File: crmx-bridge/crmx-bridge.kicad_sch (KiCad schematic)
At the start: 76 parts, among them IC101 ESP32-S3-WROOM-1U-N4R2, J101 Conn_01x18_Pin, J102 NC3FAAH2, J103 TYPEC-304S-ACP16, J104 NC3MAAH, J105 Conn_01x02_Pin, J106 Conn_01x18_Socket, Q101 DMPH4029LFGQ-13, Q102 AO3400A, U101 TIMOTWO, U102 AP63200WU, U103 ISO3088DW, U104 SRV05-4, U105 ISO3088DW

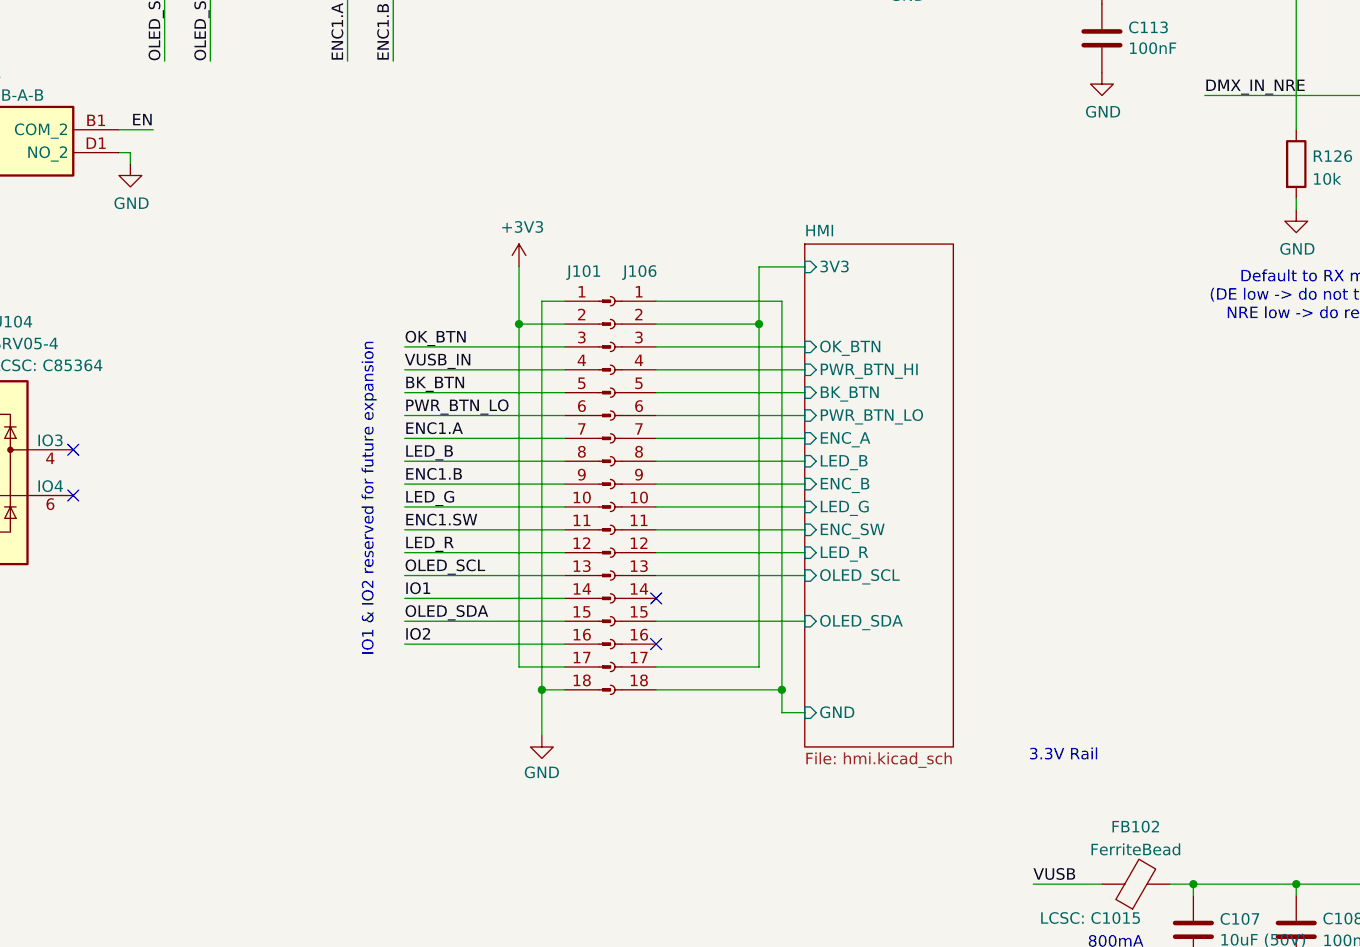
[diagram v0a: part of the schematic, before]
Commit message: updated to use FPC cable
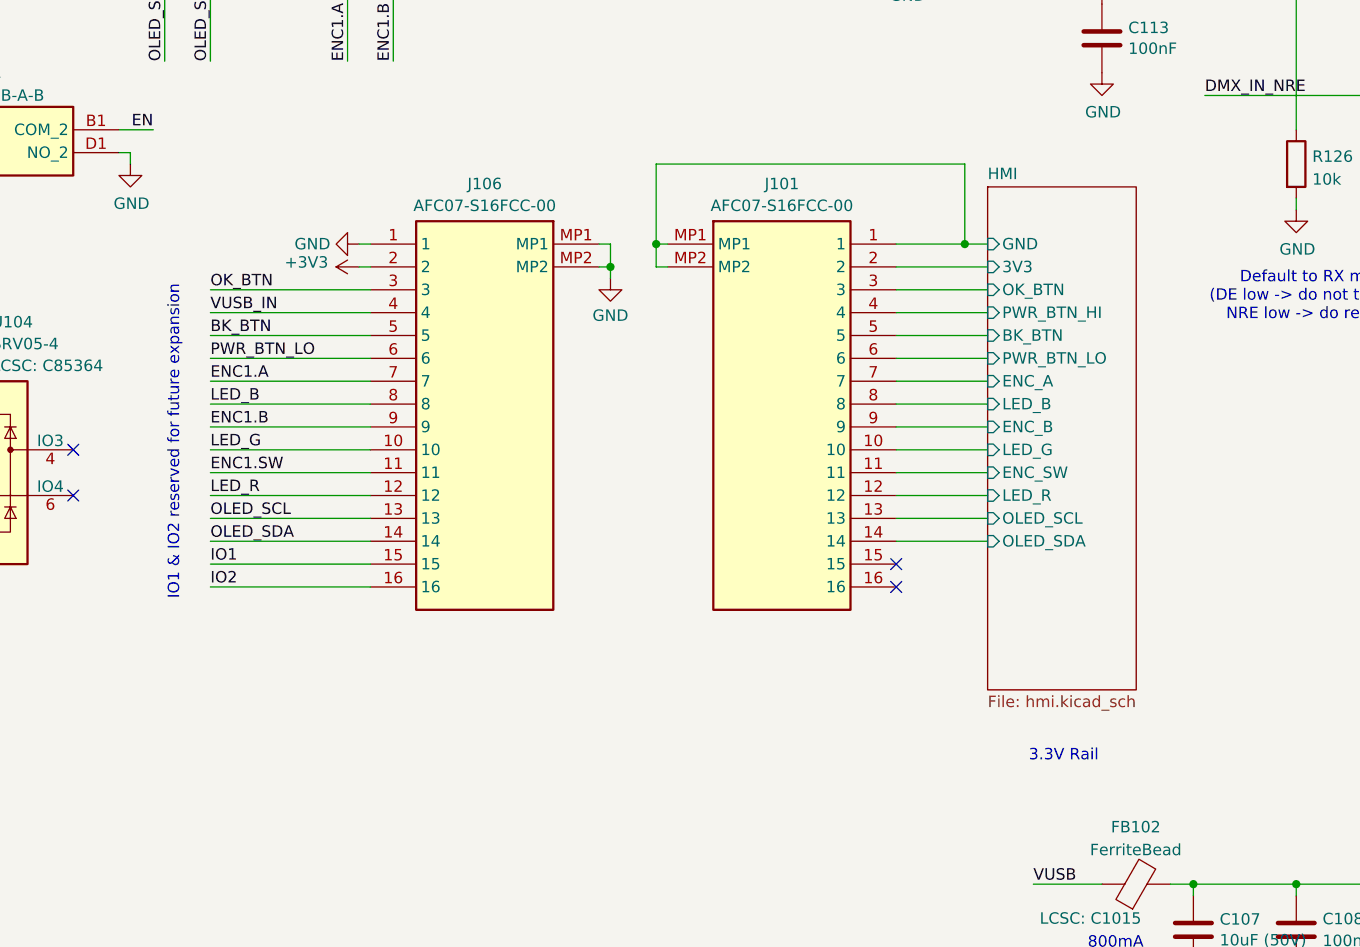
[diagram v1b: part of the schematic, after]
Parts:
- removed J101: Conn_01x18_Pin, Connector_PinSocket_1.27mm:PinSocket_2x09_P1.27mm_Vertical, symbol Connector:Conn_01x18_Pin
- removed J106: Conn_01x18_Socket, Connector_PinHeader_1.27mm:PinHeader_2x09_P1.27mm_Vertical, symbol Connector:Conn_01x18_Socket
- added J101, J106: AFC07-S16FCC-00, AFC07-S16FCC-00:AFC07S16FCC00, symbol AFC07-S16FCC-00:AFC07-S16FCC-00
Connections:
- net +3V3: now also J106.2
- net BK_BTN: now also J106.5
- net ENC1.A: now also J106.7
- net ENC1.B: now also J106.9
- net ENC1.SW: now also J106.11
- net GND: now also J106.1, J106.MP1, J106.MP2
- net HMI/3V3: now also J101.2
- net HMI/BK_BTN: now also J101.5
- net HMI/ENC_A: now also J101.7
- net HMI/ENC_B: now also J101.9
- net HMI/ENC_SW: now also J101.11
- net HMI/GND: now also J101.1, J101.MP1, J101.MP2
- net HMI/LED_B: now also J101.8
- net HMI/LED_G: now also J101.10
- net HMI/LED_R: now also J101.12
- net HMI/OK_BTN: now also J101.3
- net HMI/OLED_SCL: now also J101.13
- net HMI/OLED_SDA: now also J101.14
- net HMI/PWR_BTN_HI: now also J101.4
- net HMI/PWR_BTN_LO: now also J101.6
- net IO1: now also J106.15
- net IO2: now also J106.16
- net LED_B: now also J106.8
- net LED_G: now also J106.10
- net LED_R: now also J106.12
- net OK_BTN: now also J106.3
- net OLED_SCL: now also J106.13
- net OLED_SDA: now also J106.14
- net PWR_BTN_LO: now also J106.6
- net VUSB_IN: now also J106.4

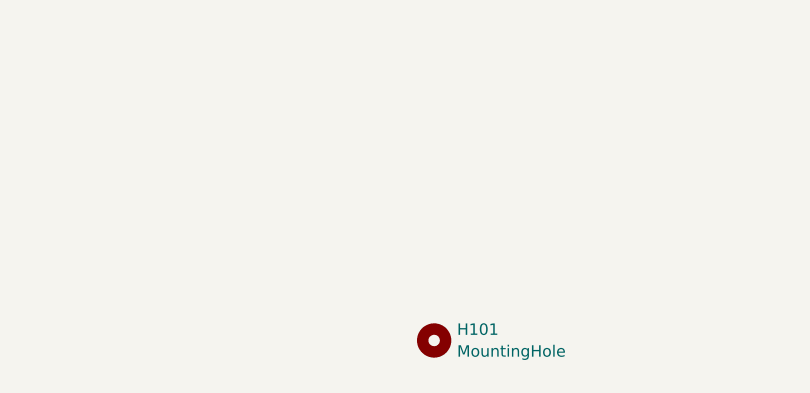
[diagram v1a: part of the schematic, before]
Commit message: Updated 3d models
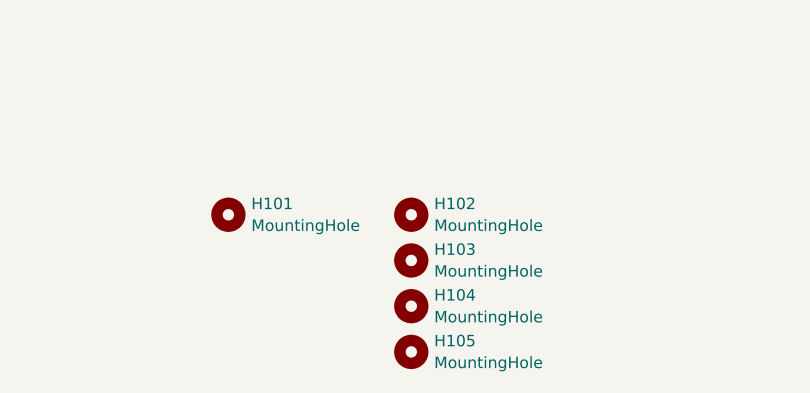
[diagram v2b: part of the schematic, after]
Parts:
- added H102, H103, H104, H105: MountingHole, MountingHole:MountingHole_3.2mm_M3, symbol Mechanical:MountingHole
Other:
- moved on the sheet: H101

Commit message: before rearranging
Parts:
- removed J103: TYPEC-304S-ACP16, LIB_TYPEC-304S-ACP16:TYPEC304SACP16, symbol TYPEC-304S-ACP16:TYPEC-304S-ACP16
- removed PS101, PS102: TEA_1-0505, Converter_DCDC:Converter_DCDC_TRACO_TEA1-xxxxE_THT, symbol Converter_DCDC:TEA1-0505E
- added J103: USB_C_Receptacle_USB2.0_16P, Connector_USB:USB_C_Receptacle_HRO_TYPE-C-31-M-12, symbol Connector:USB_C_Receptacle_USB2.0_16P
- added R125: 10R (1%), Resistor_SMD:R_0603_1608Metric, symbol Device:R
- added U106, U107: TEA1-0505, Converter_DCDC:Converter_DCDC_TRACO_TEA1-xxxx_THT, symbol Converter_DCDC:TEA1-0505
- IC101: LCSC (none) -> C3013942
- Q101: value DMPH4029LFGQ-13 -> DMP4025SFGQ-13; LCSC (none) -> C461091
- Q102: LCSC (none) -> C20917
- R103: value 133R (2%) -> 120R (1%); LCSC (none) -> C22787
- R104, R105: value 562R (2%) -> 560R (1%); LCSC (none) -> C23204
- R123: LCSC (none) -> C22787
- R132, R137, R138, R139, R140: value 50R -> 49R9; LCSC (none) -> C25120
- R134: LCSC C17168 -> (none)
- U103, U105: LCSC (none) -> C39386
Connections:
- net DMX_OUT_N: now also R125.2; no longer R103.2
- net GND: now also J103.A1 (GND), J103.A12 (GND), J103.B1 (GND), J103.B12 (GND), J103.S1 (SHIELD), U106.1 (-Vin), U107.1 (-Vin)
- net GND_ISO_1: now also U106.3 (-Vout)
- net GND_ISO_2: now also U107.3 (-Vout)
- net USB_CC1: now also J103.A5 (CC1)
- net USB_CC2: now also J103.B5 (CC2)
- net USB_DN: now also J103.A7 (D-), J103.B7 (D-)
- net USB_DP: now also J103.A6 (D+), J103.B6 (D+)
- net VCC_ISO_1: now also U106.4 (+Vout)
- net VCC_ISO_2: now also U107.4 (+Vout)
- net VUSB: now also U106.2 (+Vin), U107.2 (+Vin)
- net VUSB_IN: now also J103.A4 (VBUS), J103.A9 (VBUS), J103.B4 (VBUS), J103.B9 (VBUS)
- new net: R103.2, R125.1
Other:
- note added: "Line bias network to be RDM compliant https://getdlight.com/media/kunena/attachments/42/ANSI_E1-20_2010.pdf Ideal: 562 - 133 - 562"
- note removed: "Line bias network to be RDM compliant https://getdlight.com/media/kunena/attachments/42/ANSI_E1-20_2010.pdf"
- note removed: "TODO: - Monitor CC1 & CC2 voltages? - Make all resistors that can be 0402"
- moved on the sheet: J101, J106, R104, R105, R119, R120

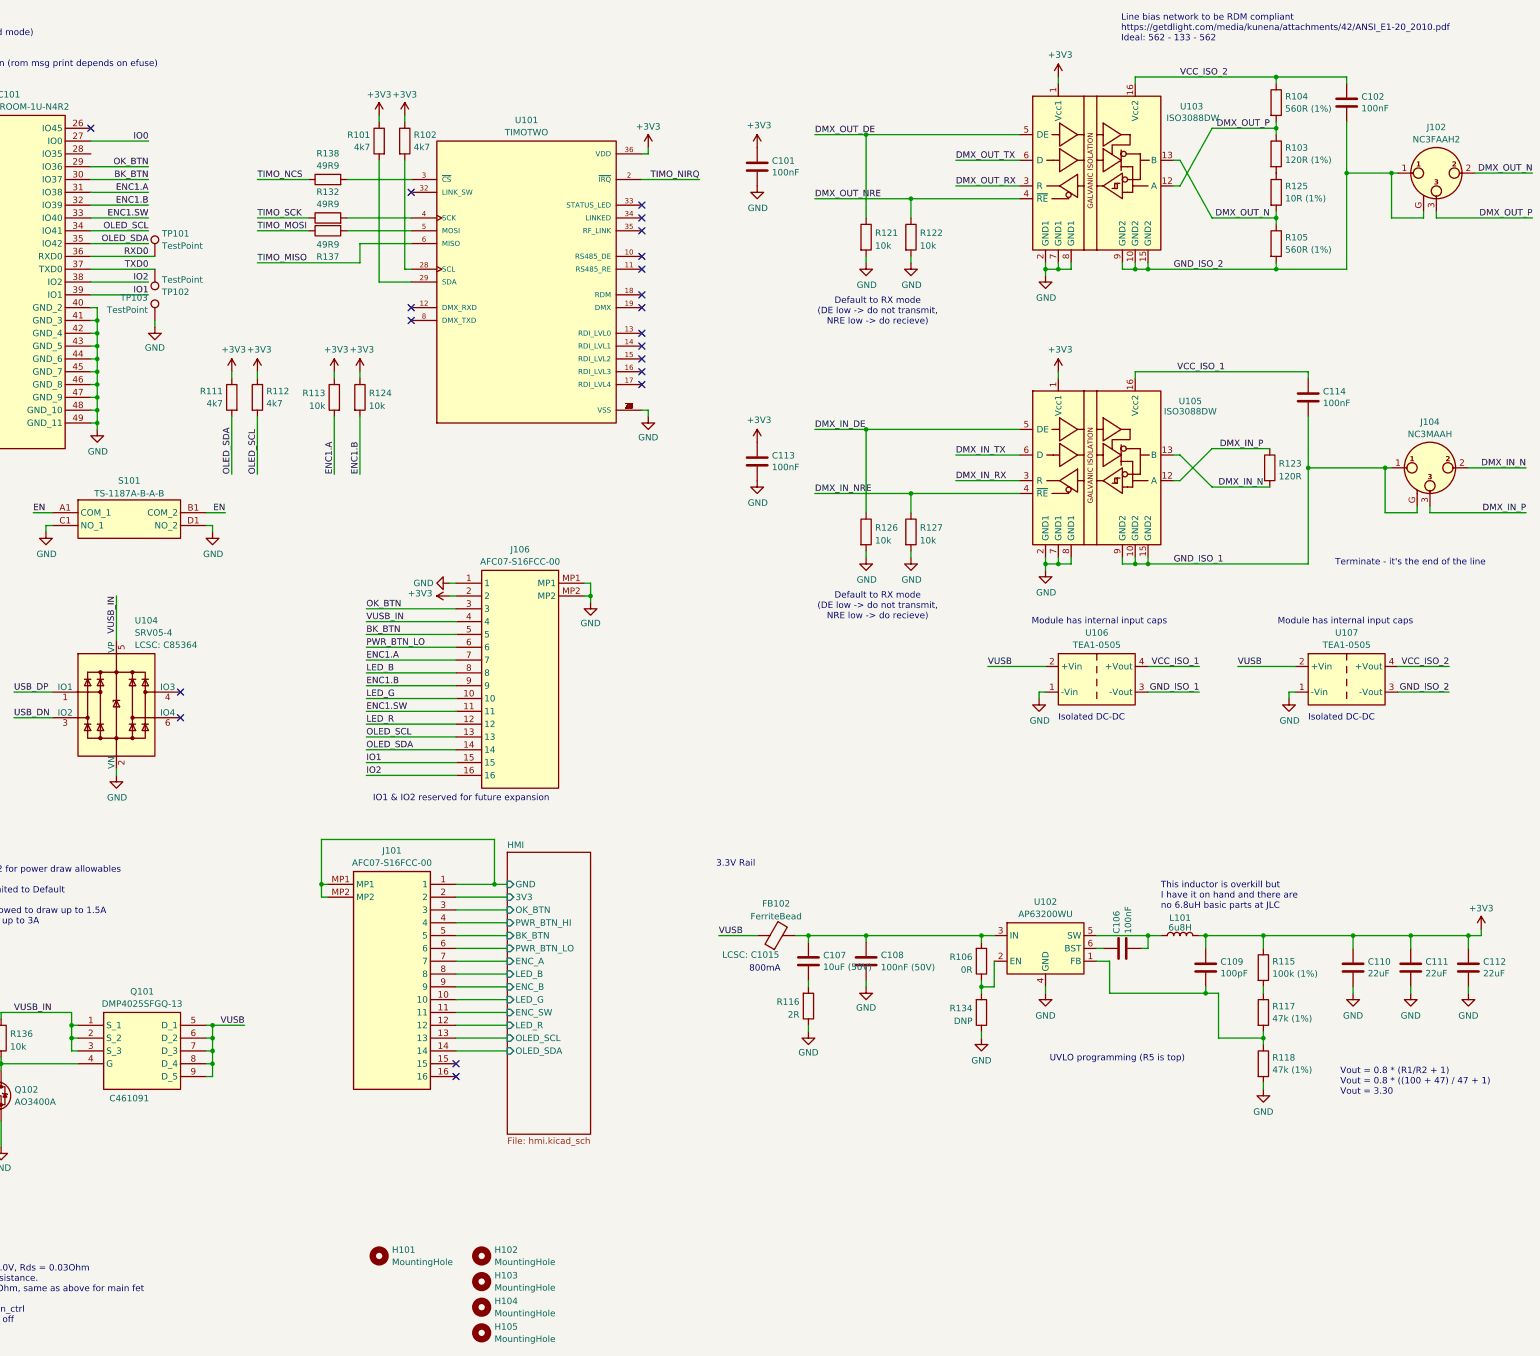
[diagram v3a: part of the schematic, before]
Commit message: Split up PCBs into separate files, Ordered V0.3
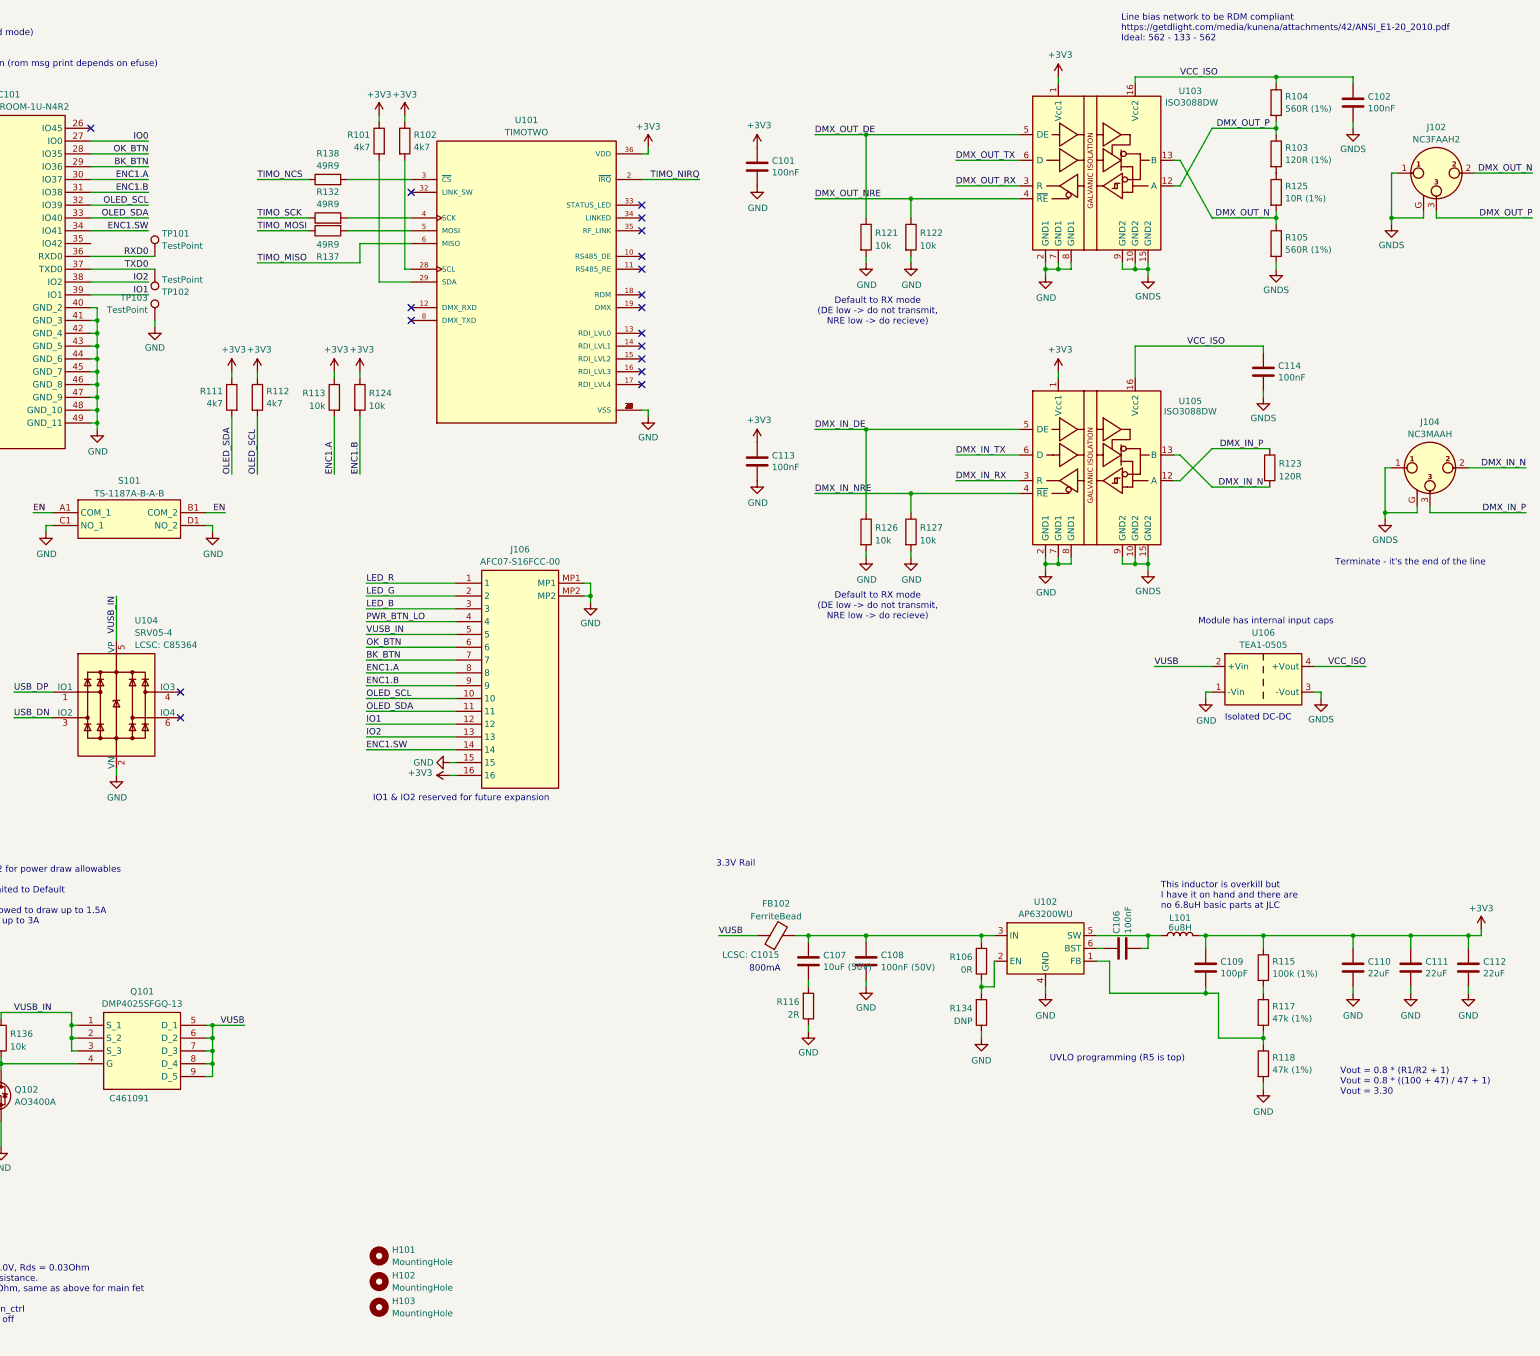
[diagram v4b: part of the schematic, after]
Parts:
- removed H104, H105: MountingHole, MountingHole:MountingHole_3.2mm_M3, symbol Mechanical:MountingHole
- removed J101: AFC07-S16FCC-00, AFC07-S16FCC-00:AFC07S16FCC00, symbol AFC07-S16FCC-00:AFC07-S16FCC-00
- removed U107: TEA1-0505, Converter_DCDC:Converter_DCDC_TRACO_TEA1-xxxx_THT, symbol Converter_DCDC:TEA1-0505
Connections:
- net GND_ISO_2 is gone; now on net GNDS: C102.2, J102.1, J102.G, R105.2, U103.10 (GND2), U103.15 (GND2), U103.9 (GND2)
- net VCC_ISO_2 is gone; now on net VCC_ISO: C102.1, R104.1, U103.16 (Vcc2)
- net +3V3: now also J106.16; no longer J106.2
- net BK_BTN: now also IC101.29 (IO36), J106.7; no longer IC101.30 (IO37), J106.5
- net ENC1.A: now also IC101.30 (IO37), J106.8; no longer IC101.31 (IO38), J106.7
- net ENC1.B: now also IC101.31 (IO38); no longer IC101.32 (IO39)
- net ENC1.SW: now also IC101.34 (IO41), J106.14; no longer IC101.33 (IO40), J106.11
- net GND: now also J106.15; no longer J106.1
- net IO1: now also J106.12; no longer J106.15
- net IO2: now also J106.13; no longer J106.16
- net LED_B: now also J106.3; no longer J106.8
- net LED_G: now also J106.2; no longer J106.10
- net LED_R: now also J106.1; no longer J106.12
- net OK_BTN: now also IC101.28 (IO35), J106.6; no longer IC101.29 (IO36), J106.3
- net OLED_SCL: now also IC101.32 (IO39), J106.10; no longer IC101.34 (IO41), J106.13
- net OLED_SDA: now also IC101.33 (IO40), J106.11; no longer IC101.35 (IO42), J106.14
- net PWR_BTN_LO: now also J106.4; no longer J106.6
- net VUSB_IN: now also J106.5; no longer J106.4
- net GND_ISO_1 renamed GNDS
- net VCC_ISO_1 renamed VCC_ISO
- no-connect marks 23 -> 21
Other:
- removed sheet HMI
- moved on the sheet: C102, C114, U106
